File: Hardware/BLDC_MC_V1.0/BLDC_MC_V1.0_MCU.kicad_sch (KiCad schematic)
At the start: 19 parts, among them J3 USB_C_Receptacle_USB2.0_16P, U4 STM32G431RBTx, Y1 7M-24.000MAAJ-T, Y2 ABS07-32.768KHZ-T

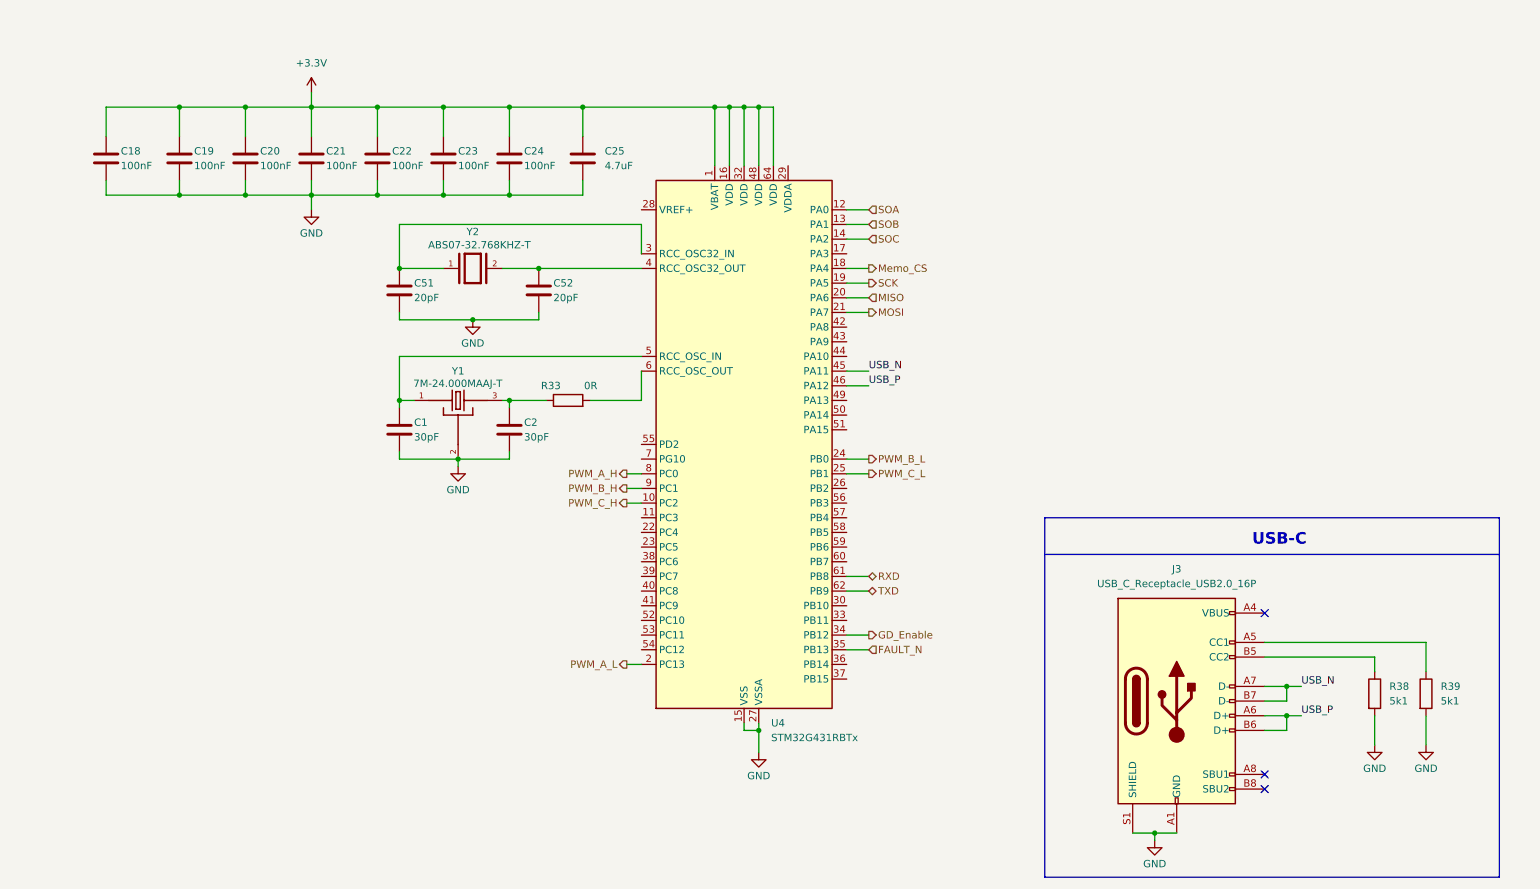
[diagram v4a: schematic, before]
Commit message: Add the JTAG debug interface
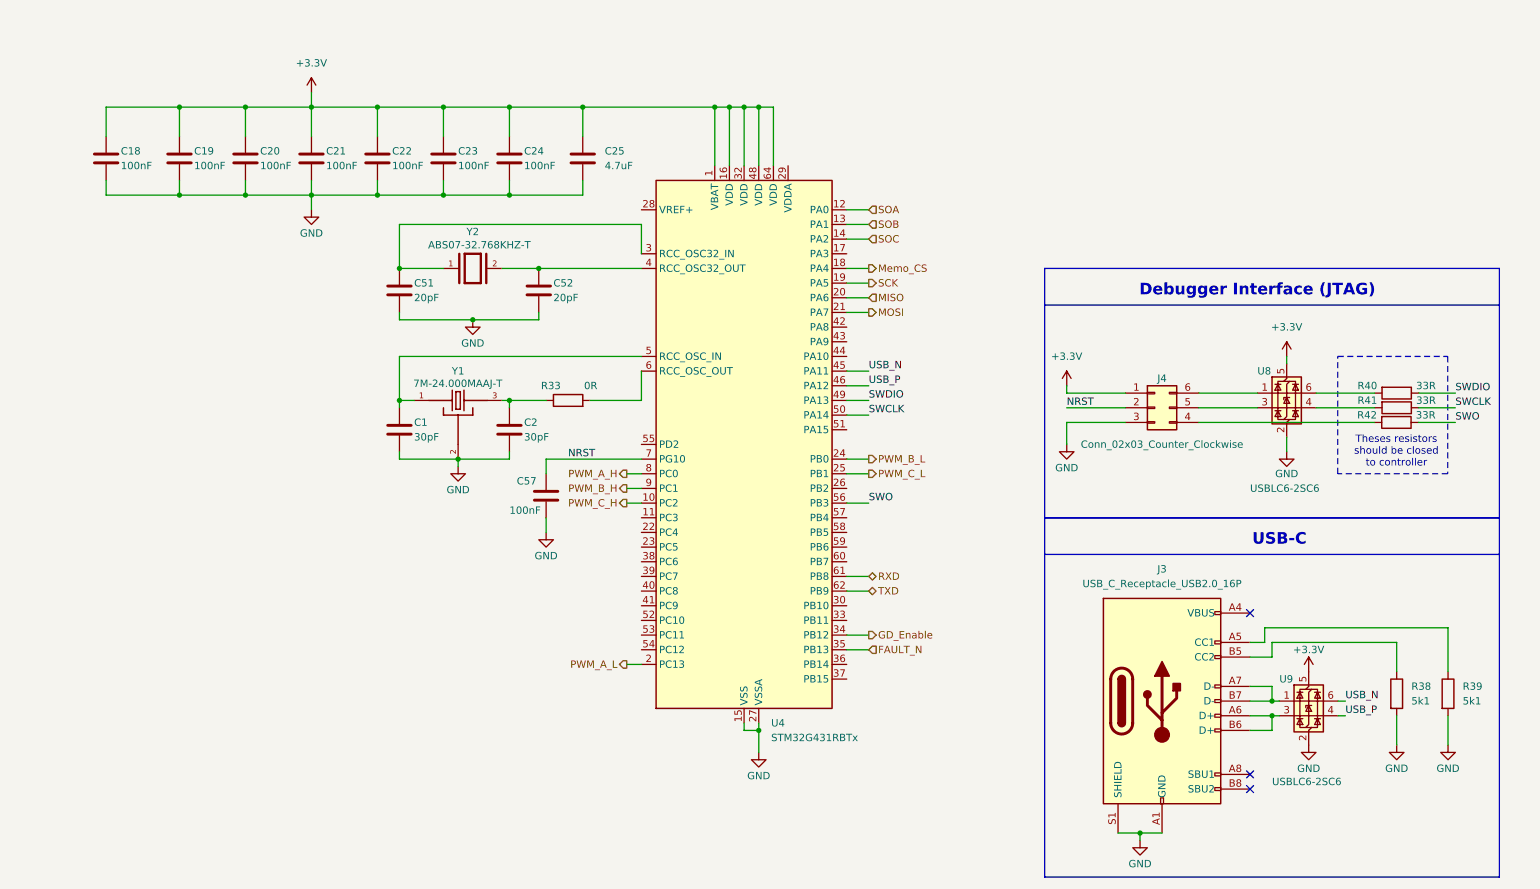
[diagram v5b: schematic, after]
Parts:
- added C57: 100nF, Capacitor_SMD:C_0805_2012Metric, symbol Device:C
- added J4: Conn_02x03_Counter_Clockwise, Connector_PinHeader_2.54mm:PinHeader_2x03_P2.54mm_Vertical, symbol Connector_Generic:Conn_02x03_Counter_Clockwise
- added R40, R41, R42: 33R, Resistor_SMD:R_0603_1608Metric, symbol Device:R
- added U8, U9: USBLC6-2SC6, Package_TO_SOT_SMD:SOT-23-6, symbol Power_Protection:USBLC6-2SC6
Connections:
- net +3.3V: now also J4.1 (Pin_1), U8.5 (VBUS), U9.5 (VBUS)
- net GND: now also C57.2, J4.3 (Pin_3), U8.2 (GND), U9.2 (GND)
- net USB_N: now also U9.6 (I/O1); no longer J3.A7 (D-), J3.B7 (D-)
- net USB_P: now also U9.4 (I/O2); no longer J3.A6 (D+), J3.B6 (D+)
- net SWDIO: now reaches U4.49 (PA13)
- net SWDIO: now also R40.1
- net SWCLK: now reaches U4.50 (PA14)
- net SWCLK: now also R41.1
- net SWO: now reaches U4.56 (PB3)
- net SWO: now also R42.1
- net NRST: now reaches U4.7 (PG10)
- net NRST: now also C57.1, J4.2 (Pin_2)
- new net: J4.6 (Pin_6), U8.1 (I/O1)
- new net: J4.5 (Pin_5), U8.3 (I/O2)
- new net: R41.2, U8.4 (I/O2)
- new net: R40.2, U8.6 (I/O1)
- new net: J3.A7 (D-), J3.B7 (D-), U9.1 (I/O1)
- new net: J3.A6 (D+), J3.B6 (D+), U9.3 (I/O2)
- new net: J4.4 (Pin_4), R42.2
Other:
- note added: "Debugger Interface (JTAG)"
- note added: "Theses resistors should be closed to controller"
- moved on the sheet: J3, R38, R39

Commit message: Add TVS for NRST and add pushbutton for rest
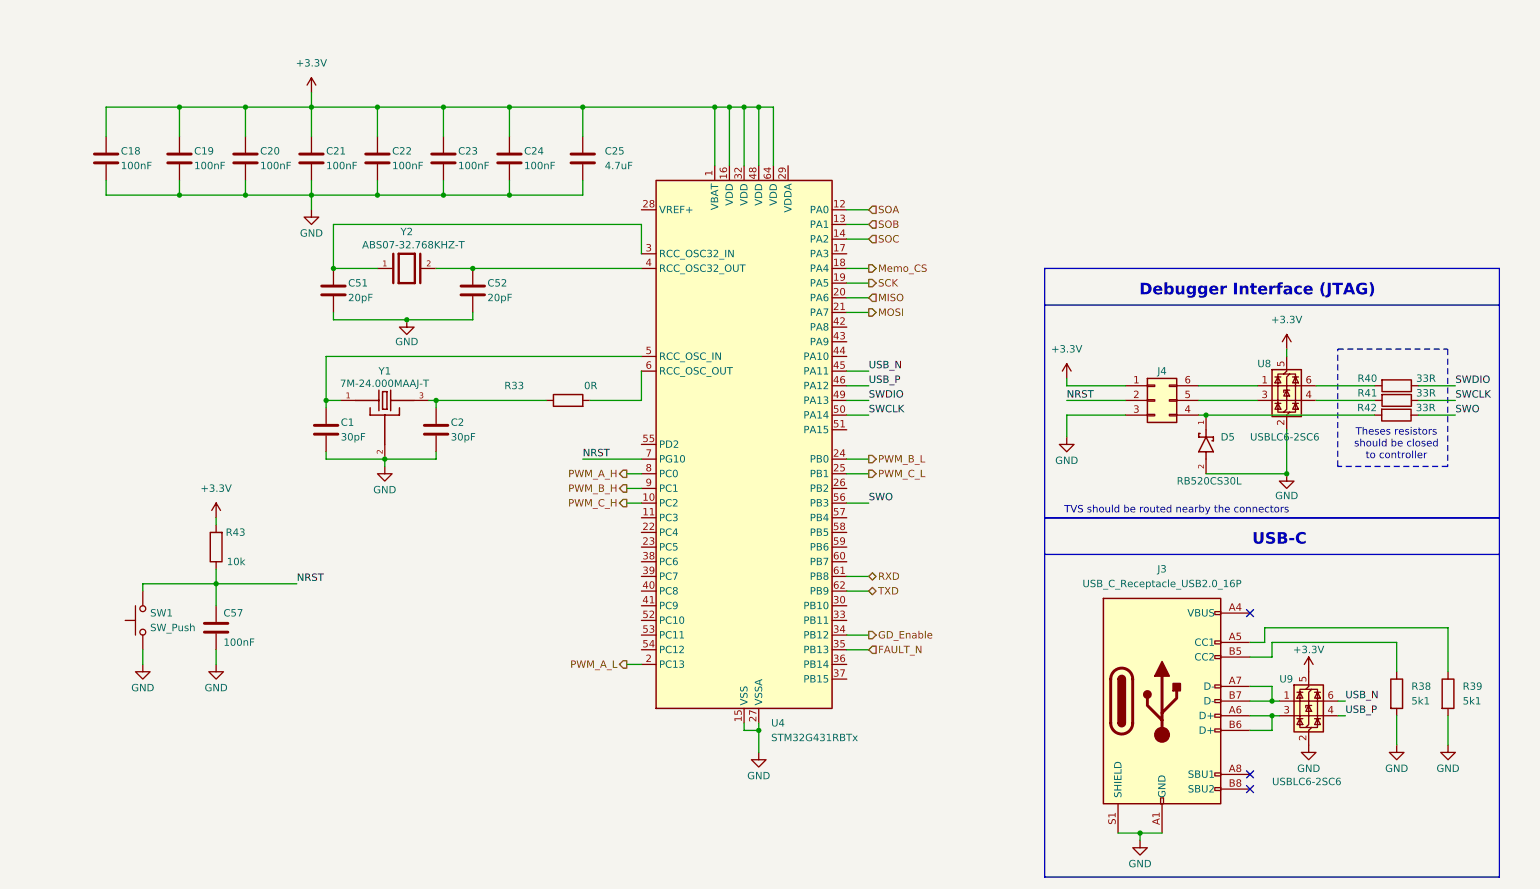
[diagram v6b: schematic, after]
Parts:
- added D5: RB520CS30L, BLDC_Motor_Driver_Components_Footprint:DIODFN98X58X50-2N, symbol RB520CS30L:RB520CS30L
- added R43: 10k, Resistor_SMD:R_0603_1608Metric, symbol Device:R
- added SW1: SW_Push, Button_Switch_SMD:SW_Push_1P1T_NO_E-Switch_TL3301NxxxxxG, symbol Switch:SW_Push
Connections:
- net +3.3V: now also R43.2
- net GND: now also D5.2, SW1.1
- net NRST: now also R43.1, SW1.2
- net at J4.4 (Pin_4), R42.2: now also D5.1
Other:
- note added: "TVS should be routed nearby the connectors"
- moved on the sheet: C1, C2, C51, C52, C57, J4, R40, R41, R42, U8, Y1, Y2

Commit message: Add the new bipolar TVS for the debugger connector
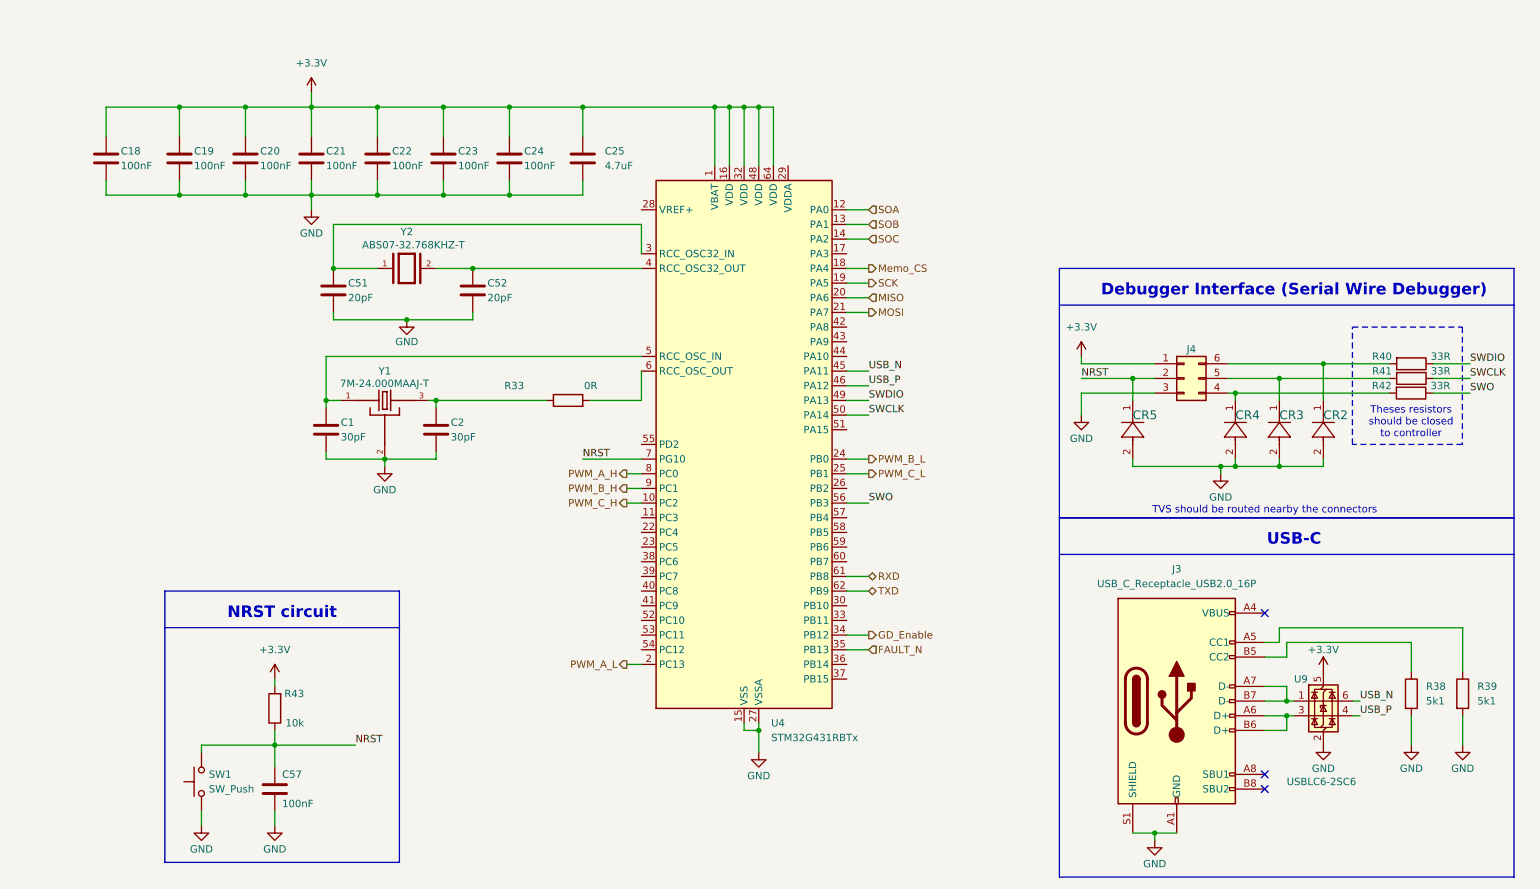
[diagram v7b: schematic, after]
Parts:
- removed D5: RB520CS30L, BLDC_Motor_Driver_Components_Footprint:DIODFN98X58X50-2N, symbol RB520CS30L:RB520CS30L
- removed U8: USBLC6-2SC6, Package_TO_SOT_SMD:SOT-23-6, symbol Power_Protection:USBLC6-2SC6
- added CR2, CR3, CR4, CR5: PESD3V3L1BA_115, BLDC_Motor_Driver_Components_Footprint:DIODE_PESD3V3L1BA_115_NEX, symbol PESD3V3L1BA,115:PESD3V3L1BA_115
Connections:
- net GND: now also CR2.2, CR3.2, CR4.2, CR5.2
- net NRST: now also CR5.1
- net at J4.6 (Pin_6): now also R40.2, CR2.1
- net at J4.5 (Pin_5): now also R41.2, CR3.1
- net at J4.4 (Pin_4), R42.2: now also CR4.1
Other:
- note added: "Debugger Interface (Serial Wire Debugger)"
- note added: "NRST circuit"
- note removed: "Debugger Interface (JTAG)"
- moved on the sheet: C57, J3, J4, R38, R39, R40, R41, R42, R43, SW1, U9

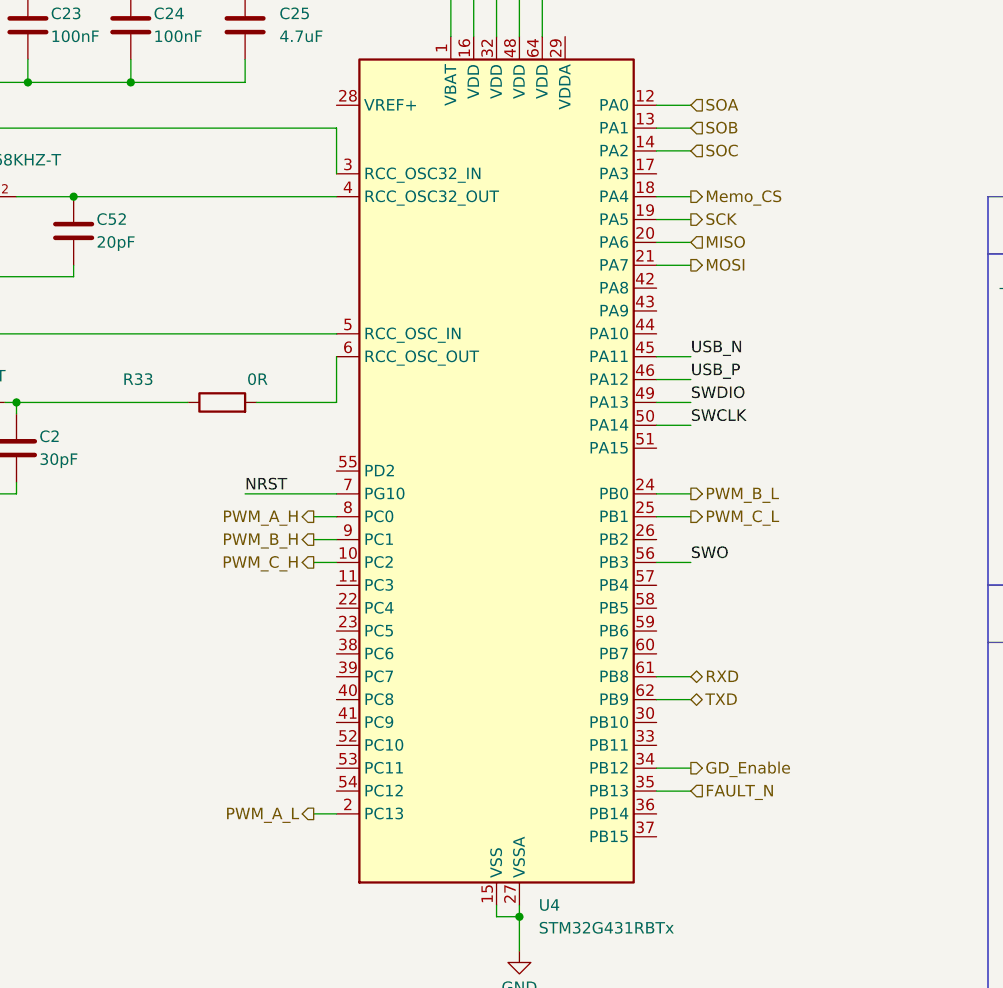
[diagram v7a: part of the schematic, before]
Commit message: Edit the sch of the project by adding the hall sensor sheet and interface with the MCU sheet and annotate the components in memory sheet
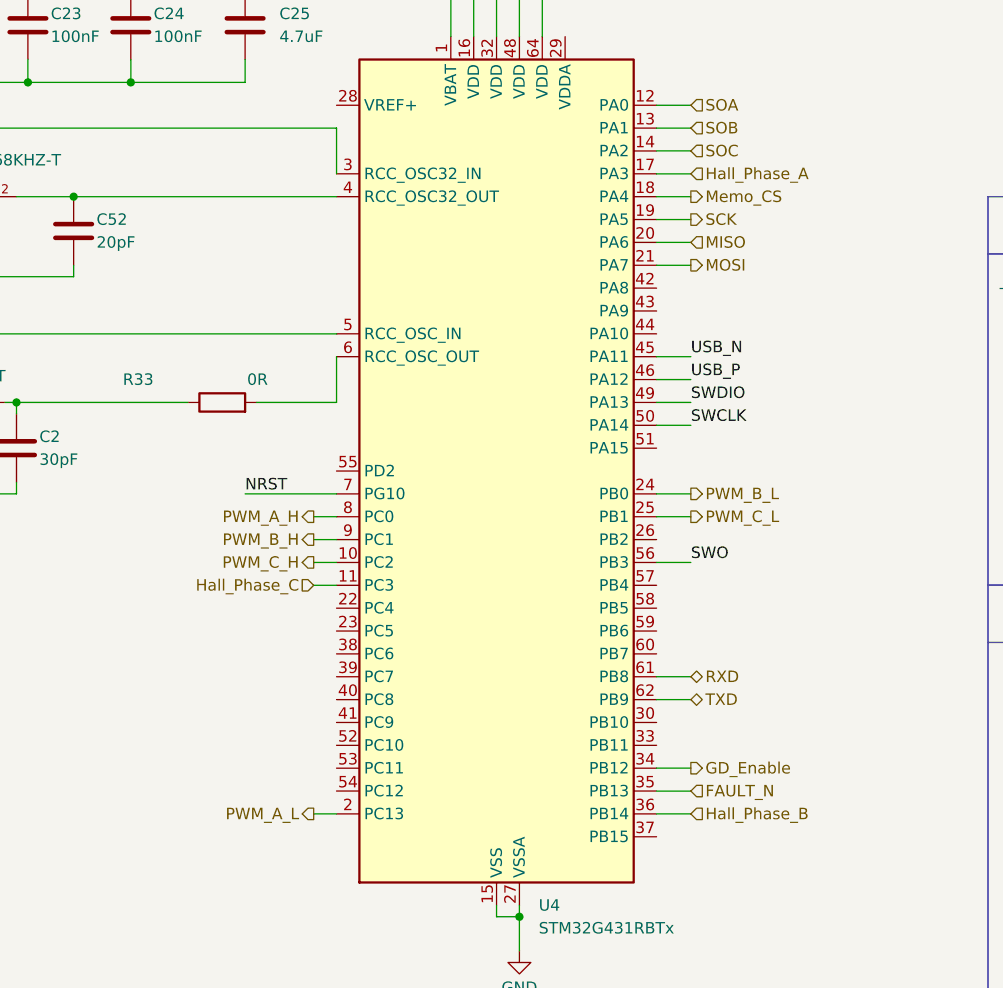
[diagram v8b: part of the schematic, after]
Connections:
- net Hall_Phase_C: now reaches U4.11 (PC3)
- net Hall_Phase_A: now reaches U4.17 (PA3)
- net Hall_Phase_B: now reaches U4.36 (PB14)
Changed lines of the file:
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@@
+	(wire
+		(pts
+			(xy 129.54 102.87) (xy 132.08 102.87)
+		)
+		(stroke
+			(width 0)
+			(type default)
+		)
+	)
 	(wire
 		(pts
@@
 	(wire
 		(pts
+			(xy 167.64 128.27) (xy 171.45 128.27)
+		)
+		(stroke
+			(width 0)
+			(type default)
+		)
+	)
+	(wire
+		(pts
 			(xy 167.64 59.69) (xy 171.45 59.69)
 		)
@@
 		(pts
 			(xy 129.54 97.79) (xy 132.08 97.79)
+		)
+		(stroke
+			(width 0)
+			(type default)
+		)
+	)
+	(wire
+		(pts
+			(xy 167.64 57.15) (xy 171.45 57.15)
 		)
 		(stroke
@@
 		)
 	)
+	(hierarchical_label "Hall_Phase_A"
+		(shape input)
+		(at 171.45 57.15 0)
+		(effects
+			(font
+				(size 1.27 1.27)
+			)
+			(justify left)
+		)
+	)
 	(hierarchical_label "TXD"
 		(shape bidirectional)
@@
 		)
 	)
+	(hierarchical_label "Hall_Phase_B"
+		(shape input)
+		(at 171.45 128.27 0)
+		(effects
+			(font
+				(size 1.27 1.27)
+			)
+			(justify left)
+		)
+	)
 	(hierarchical_label "FAULT_N"
 		(shape input)
@@
 		)
 	)
+	(hierarchical_label "Hall_Phase_C"
+		(shape input)
+		(at 129.54 102.87 180)
+		(effects
+			(font
+				(size 1.27 1.27)
+			)
+			(justify right)
+		)
+	)
